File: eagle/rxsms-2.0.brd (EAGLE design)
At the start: 160 x 100 mm, 13 parts, among them U1 MAX3232ESE, U2 XMEGA-A4UTQFP, X1 PN61729-S

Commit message: continued schematics
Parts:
- added C10, C11: opt, rcl:C0805K
- added C12, C13: 4u7/50V, rcl:C0805K
- added C14, C15: 22u/16V, rcl:C0805K
- added C16, C21, C22, C23, C24, C25, C26, C27, C28, C29, C6, C7, C8, C9: 100n, rcl:C0805K
- added C17, C18, C19, C20: >100n/low ESR, rcl:C0805K
- added Q1: opt, crystal:HC49/S
- added Q2, Q3, Q4: BSS123, transistor-small-signal:SOT23
- added R1, R10, R11, R2, R3, R4, R5, R6, R8, R9: 10k, rcl:R0805
- added R12, R13, R14, R15: 24/1%, rcl:R0805
- added R16, R17, R18, R19, R20: 1k, rcl:R0805
- added R7: 100k, rcl:R0805
- added T1, T2, T3, T4, T5: SMS_IP67, SMSIp67:IP67
- added U$3: AVR-PDIVERT, avr-7:AVR-ISP-6
- added U$4: UDN2596, UDN2596:DIL20
- added U$5: SP490, SP491:SO08
- added U$6: BTS6143, BTS6134:TO-252-5-1
- added U$7, U$8, U$9: (no value), poti:VERT_POTI
- added U3: TSR_1-2450, _traco_tsr-1:TSR-1
- added U4: LM1117, LM1117:TO252
- added U5: TMV_0505EN, _traco_tmv-1:TMV-EN
- added U6: ADUM3160, adum3160:SO-16W
- added U7: TPS73125, TPS731xx:SOT25
- moved X1 394.7 mm to (-191.8, -289.6), turned to 0 degrees
- moved X4 288.8 mm to (-80.0, -123.2)
- moved U2 44.4 mm to (-87.6, 22.9), turned to 180 degrees
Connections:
- removed net AVCC: U2.39
- removed net VCC: U2.19, U2.31, U2.9
- new net !EXP_LO: U$4.16, X4.5
- new net !EXP_SODS: U$4.15, X4.3
- new net !EXP_SOE: U$4.17, X4.4
- new net !SIM_LO: R4.1, U$4.19
- new net !SIM_SODS: R2.1, U$4.13
- new net !SIM_SOE: R3.1, U$4.18
- new net +28V_EXP: U$4.10, U$6.PIN1, U$6.PIN5, X4.1, X4.9
- new net +28V_SUPPLY: C12.1, U$6.TAB
- new net +3V3: C15.1, C19.1, C20.1, C6.1, C7.1, C8.1, C9.1, Q3.1, Q4.1, R1.1, R10.2, R2.2, R3.2, R4.2, R8.2, U$3.2, U$4.20, U2.19, U2.31, U2.39, U2.9, U4.3, U6.12, U6.13, U6.14, U6.16
- new net +5V: C13.1, C14.1, C16.1, R11.2, R9.2, U$5.1, U3.3, U4.2, U5.1, U7.1, U7.3
- new net ADC_POTI_BIT_ERROR_RATE: C22.1, U$7.P2
- new net ADC_POTI_DROP_DURATION: C24.1, U$9.P2
- new net ADC_POTI_DROP_RATE: C23.1, U$8.P2
- new net EXPPWR_EN: Q2.1, R5.2
- new net EXP_CHG_IN: X4.2
- new net EXP_CHG_RET: X4.12
- new net EXP_SERIAL_FROM_EXP+: R6.2, U$5.8, X4.13
- new net EXP_SERIAL_FROM_EXP-: R6.1, U$5.7, X4.14
- new net EXP_SERIAL_TO_EXP+: R7.1, U$5.5, X4.6
- new net EXP_SERIAL_TO_EXP-: R7.2, U$5.6, X4.7
- new net N$11: C10.1, Q1.1, U2.37
- new net N$12: C11.1, Q1.2, U2.36
- new net N$13: U$3.1, U2.34
- new net N$14: R1.2, U$3.5, U2.35
- new net N$15: C17.2, C18.2, U6.2, U6.8, X1.4, X1.S1, X1.S2
- new net N$16: Q2.3, U$6.PIN2
- new net N$17: C18.1, U6.1, X1.1
- new net N$18: C17.1, U6.3, U6.4, U6.5
- new net N$19: R12.1, U6.6
- new net N$20: Q3.3, R9.1, U$5.2
- new net N$21: Q4.3, R11.1, U$5.3
- new net N$22: R13.1, U6.7
- new net N$23: R13.2, X1.3
- new net N$24: R12.2, X1.2
- new net N$25: C21.1, U7.4
- new net N$26: C25.2, T1.1, T1.2
- new net N$27: C26.2, T2.1, T2.2
- new net N$28: R17.1, T2.3, T2.4
- new net N$29: R14.2, U6.9
- new net N$30: R15.2, U6.10
- new net N$31: R16.1, T1.3, T1.4
- new net N$32: C27.2, T3.1, T3.2
- new net N$33: R18.1, T3.3, T3.4
- new net N$34: C28.2, T4.1, T4.2
- new net N$35: R19.1, T4.3, T4.4
- new net N$36: C29.2, T5.1, T5.2
- new net N$37: R20.1, T5.3, T5.4
- new net N$38: U$7.P3, U$8.P3, U$9.P3, U7.5
- new net SW_ERRINH: C29.1, R20.2
- new net SW_LO: C25.1, R16.2
- new net SW_PWR: C28.1, R19.2
- new net SW_SODS: C27.1, R18.2
- new net SW_SOE: C26.1, R17.2
- new net UART_EXP_RX: Q3.2, R8.1
- new net UART_EXP_TX: Q4.2, R10.1
- new net USB-D+: R15.1
- new net USB_D-: R14.1
- net GND: now also C10.2, C11.2, C12.2, C13.2, C14.2, C15.2, C16.2, C19.2, C20.2, C21.2, C22.2, C23.2, C24.2, C6.2, C7.2, C8.2, C9.2, Q2.2, R5.1, U$3.6, U$4.12, U$4.2, U$5.4, U$7.P1, U$8.P1, U$9.P1, U3.2, U4.1, U5.2, U6.11, U6.15, U7.2, X4.15, X4.8, X4.G1, X4.G2
- net VDD: now also U5.5
- net VSS: now also U5.7

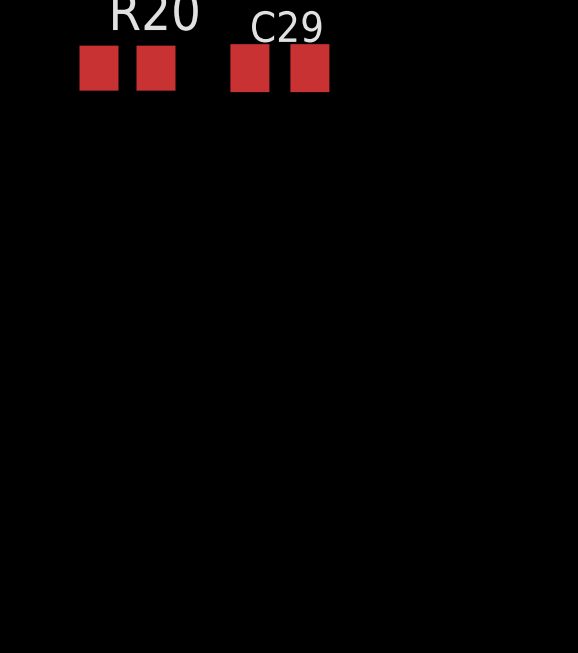
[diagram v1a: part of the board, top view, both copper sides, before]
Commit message: capacitors for isolating DCDC converter added
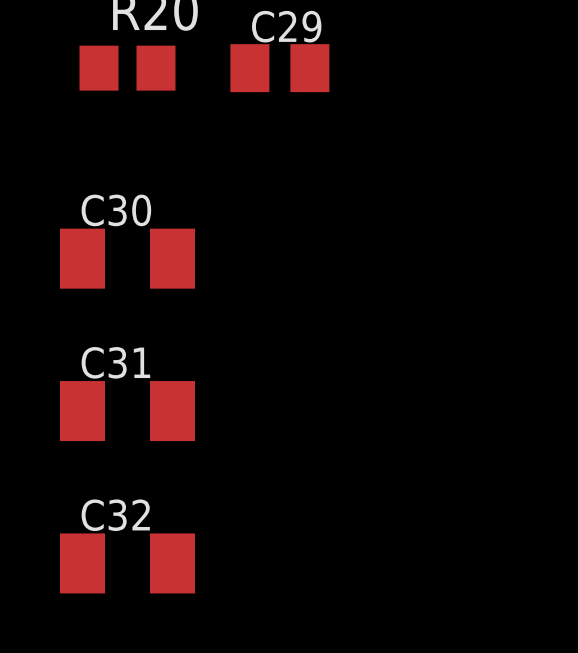
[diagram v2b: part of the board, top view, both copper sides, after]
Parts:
- added C30, C31, C32: 10u/16V, rcl:C1206K
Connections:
- new net +VIN: C31.1, U5.1
- net +5V: now also C30.1; no longer U5.1
- net GND: now also C30.2, C31.2
- net VDD: now also C32.1
- net VSS: now also C32.2
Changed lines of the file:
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@@
 <element name="R20" library="rcl" package="R0805" value="1k" x="-224.79" y="-469.9"/>
 <element name="C29" library="rcl" package="C0805K" value="100n" x="-219.71" y="-469.9"/>
+<element name="C30" library="rcl" package="C1206K" value="10u/16V" x="-224.79" y="-476.25"/>
+<element name="C31" library="rcl" package="C1206K" value="10u/16V" x="-224.79" y="-481.33"/>
+<element name="C32" library="rcl" package="C1206K" value="10u/16V" x="-224.79" y="-486.41"/>
 </elements>
 <signals>
@@
 <contactref element="C23" pad="2"/>
 <contactref element="C24" pad="2"/>
+<contactref element="C30" pad="2"/>
+<contactref element="C31" pad="2"/>
 <wire x1="-210.76" y1="-306.91" x2="-196.85" y2="-306.1" width="0" layer="19" extent="1-1"/>
 <wire x1="-211.09" y1="-311.15" x2="-210.76" y2="-306.91" width="0" layer="19" extent="1-1"/>
@@
 <wire x1="-81.83" y1="24.46" x2="-88.43" y2="28.66" width="0" layer="19" extent="1-1"/>
 <wire x1="-154.305" y1="-146.5834" x2="-131.76" y2="-175.26" width="0" layer="19" extent="1-1"/>
+<wire x1="-223.29" y1="-476.25" x2="-211.09" y2="-365.76" width="0" layer="19" extent="1-1"/>
+<wire x1="-223.29" y1="-481.33" x2="-223.29" y2="-476.25" width="0" layer="19" extent="1-1"/>
 </signal>
 <signal name="VSS">
@@
 <contactref element="X2" pad="G2"/>
 <contactref element="U5" pad="7"/>
+<contactref element="C32" pad="2"/>
+<wire x1="-83.82" y1="-78.74" x2="-223.29" y2="-486.41" width="0" layer="19" extent="1-1"/>
 <wire x1="11.43" y1="12.8778" x2="-83.82" y2="-78.74" width="0" layer="19" extent="1-1"/>
 <wire x1="12.7" y1="30.8864" x2="11.43" y2="12.8778" width="0" layer="19" extent="1-1"/>
@@
 <contactref element="C1" pad="1"/>
 <contactref element="U5" pad="5"/>
+<contactref element="C32" pad="1"/>
+<wire x1="-88.9" y1="-78.74" x2="-226.29" y2="-486.41" width="0" layer="19" extent="1-1"/>
 <wire x1="-49.26" y1="80.01" x2="-88.9" y2="-78.74" width="0" layer="19" extent="1-1"/>
 <wire x1="-42.545" y1="84.3534" x2="-49.26" y2="80.01" width="0" layer="19" extent="1-1"/>
@@
 <contactref element="C13" pad="1"/>
 <contactref element="C14" pad="1"/>
-<contactref element="U5" pad="1"/>
 <contactref element="U$5" pad="1"/>
 <contactref element="C16" pad="1"/>
@@
 <contactref element="U7" pad="1"/>
 <contactref element="U7" pad="3"/>
+<contactref element="C30" pad="1"/>
 <wire x1="-195.9" y1="-306.1" x2="-197.8" y2="-306.1" width="0" layer="19" extent="1-1"/>
 <wire x1="-175.52" y1="-298.17" x2="-195.9" y2="-306.1" width="0" layer="19" extent="1-1"/>
@@
 <wire x1="-131.81" y1="-194.31" x2="-129.86" y2="-214.63" width="0" layer="19" extent="1-1"/>
 <wire x1="-158.115" y1="-146.5834" x2="-131.81" y2="-194.31" width="0" layer="19" extent="1-1"/>
-<wire x1="-99.06" y1="-78.74" x2="-158.115" y2="-146.5834" width="0" layer="19" extent="1-1"/>
-<wire x1="-101.33" y1="-66.04" x2="-99.06" y2="-78.74" width="0" layer="19" extent="1-1"/>
+<wire x1="-101.33" y1="-66.04" x2="-158.115" y2="-146.5834" width="0" layer="19" extent="1-1"/>
 <wire x1="-101.33" y1="-60.96" x2="-101.33" y2="-66.04" width="0" layer="19" extent="1-1"/>
 <wire x1="-82.55" y1="-48.26" x2="-101.33" y2="-60.96" width="0" layer="19" extent="1-1"/>
+<wire x1="-226.29" y1="-476.25" x2="-197.8" y2="-306.1" width="0" layer="19" extent="1-1"/>
 </signal>
 <signal name="!SIM_LO">
@@
 <wire x1="-205.76" y1="-351.36" x2="-205.76" y2="-332.31" width="0" layer="19" extent="1-1"/>
 </signal>
+<signal name="+VIN">
+<contactref element="U5" pad="1"/>
+<contactref element="C31" pad="1"/>
+<wire x1="-99.06" y1="-78.74" x2="-226.29" y2="-481.33" width="0" layer="19" extent="1-1"/>
+</signal>
 </signals>

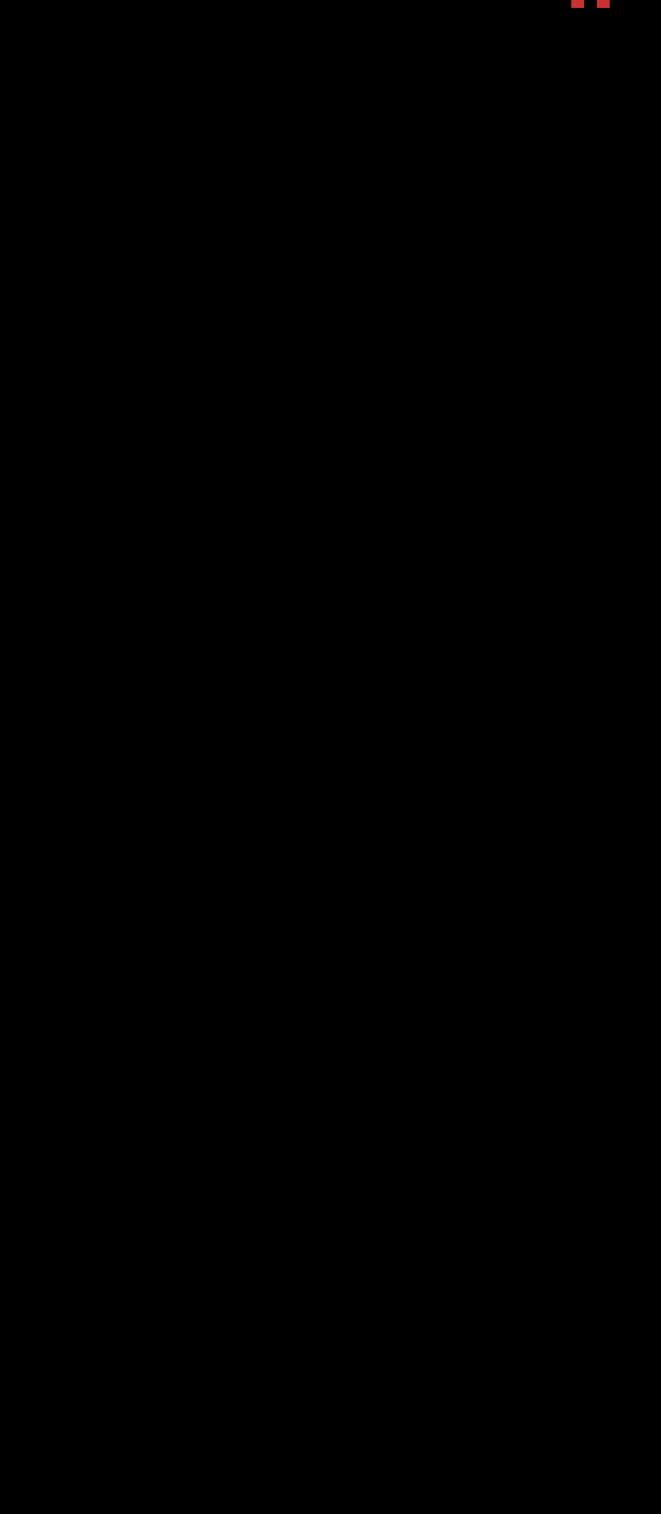
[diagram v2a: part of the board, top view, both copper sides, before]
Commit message: added optocouplers for MAX3232
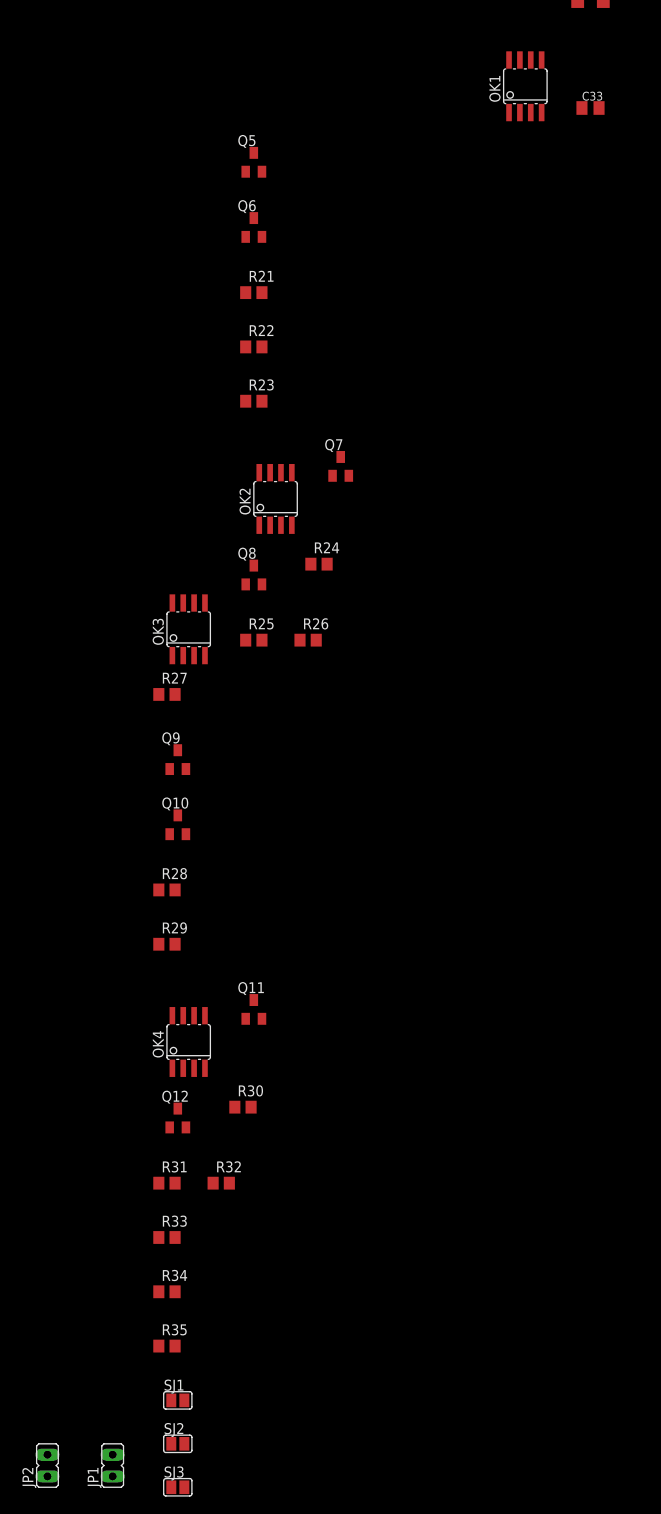
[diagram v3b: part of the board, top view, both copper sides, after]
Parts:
- added C33: 100n, rcl:C0805K
- added JP1, JP2: (no value), jumper:JP1
- added OK1, OK2, OK3, OK4: HCPL0600, optocoupler:SOIC08
- added Q10, Q11, Q12, Q5, Q6, Q7, Q8, Q9: BSS123, transistor-small-signal:SOT23
- added R21, R23, R24, R26, R27, R28, R30, R31: 10k, rcl:R0805
- added R22, R25: 127, rcl:R0805
- added R29, R32: 267, rcl:R0805
- added R33, R34, R35: opt, rcl:R0805
- added SJ1, SJ2, SJ3: (no value), jumper:SJ
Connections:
- new net ADC_REF: C33.1, U$7.P3, U$8.P3, U$9.P3, U7.5
- new net DEBUG_RX_D-: R33.1
- new net DEBUG_TX_D+: R35.1
- new net N$39: OK1.6, R23.1, U1.11
- new net N$40: Q5.1, Q6.3, R21.1
- new net N$41: Q11.1, Q12.3, R31.1
- new net N$42: OK1.2, R22.1
- new net N$43: OK2.3, Q7.3
- new net N$44: OK2.2, R25.1
- new net N$45: OK2.6, R26.1, U1.10
- new net N$46: Q7.1, Q8.3, R24.1
- new net N$47: Q10.3, Q9.1, R28.1
- new net N$48: OK3.3, Q9.3
- new net N$49: OK4.3, Q11.3
- new net N$50: OK3.2, R29.1
- new net N$51: OK4.2, R32.1
- new net N$52: Q10.1, U1.12
- new net N$53: Q12.1, U1.9
- new net N$54: OK4.6, R30.1, R33.2
- new net N$55: Q8.1, R34.2, R35.2
- new net N$56: SJ1.2, X2.G2
- new net N$57: SJ2.2, X3.G2
- new net N$58: SJ3.2, X4.G2
- new net N$59: JP1.2, JP2.1, R34.1
- new net UART_GND_RX: OK3.6, R27.1
- new net UART_GND_TX: Q6.1
- net +3V3: now also OK3.7, OK3.8, OK4.7, OK4.8, R21.2, R22.2, R24.2, R25.2, R27.2, R30.2
- net GND: now also C33.2, OK3.5, OK4.5, Q5.2, Q6.2, Q7.2, Q8.2, SJ3.1; no longer X4.G1, X4.G2
- net N$38: now also OK1.3, Q5.3; no longer U$7.P3, U$8.P3, U$9.P3, U7.5
- net UART_EXP_RX: now also JP1.1
- net UART_EXP_TX: now also JP2.2
- net VDD: now also OK1.7, OK1.8, OK2.7, OK2.8, R23.2, R26.2, R28.2, R29.2, R31.2, R32.2
- net VSS: now also OK1.5, OK2.5, Q10.2, Q11.2, Q12.2, Q9.2, SJ1.1, SJ2.1; no longer X2.G1, X2.G2, X3.G1, X3.G2

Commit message: added RX EXP charging line to debug serial DSUB
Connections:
- net EXP_CHG_IN: now also X3.1, X3.6, X3.7
- net EXP_CHG_RET: now also X3.4, X3.8, X3.9
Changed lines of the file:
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@@
 <signal name="EXP_CHG_IN">
 <contactref element="X4" pad="2"/>
+<contactref element="X3" pad="1"/>
+<contactref element="X3" pad="6"/>
+<contactref element="X3" pad="7"/>
+<wire x1="12.7" y1="68.1736" x2="-81.28" y2="-116.332" width="0" layer="19" extent="1-1"/>
+<wire x1="10.16" y1="69.5452" x2="12.7" y2="68.1736" width="0" layer="19" extent="1-1"/>
+<wire x1="10.16" y1="72.2884" x2="10.16" y2="69.5452" width="0" layer="19" extent="1-1"/>
 </signal>
 <signal name="EXP_CHG_RET">
 <contactref element="X4" pad="12"/>
+<contactref element="X3" pad="4"/>
+<contactref element="X3" pad="8"/>
+<contactref element="X3" pad="9"/>
+<wire x1="10.16" y1="75.0316" x2="-78.74" y2="-123.19" width="0" layer="19" extent="1-1"/>
+<wire x1="10.16" y1="77.7748" x2="10.16" y2="75.0316" width="0" layer="19" extent="1-1"/>
+<wire x1="12.7" y1="76.4032" x2="10.16" y2="75.0316" width="0" layer="19" extent="1-1"/>
 </signal>
 <signal name="N$17">

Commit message: second set of buttons and LEDs added
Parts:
- added LED1, LED2, LED3, LED4, LED5, LED6, LED7, LED8: (no value), led:CHIPLED_1206
- added R36, R37, R38, R39, R40, R41, R42, R43, R44, R45, R46, R47: 220, rcl:R0805
- added T10, T6, T7, T8: SWITCH_LED, mentor-switch:SWITCH_LED
- added T9: SMS_IP67, SMSIp67:IP67
- T3: value SMS_IP67 -> SWITCH_LED; device SMSIp67:IP67 -> mentor-switch:SWITCH_LED
- moved T1 495.7 mm to (-349.2, -838.2)
- moved T4 418.8 mm to (-336.6, -838.2)
- moved T5 393.4 mm to (-323.9, -838.2)
- moved R16 371.5 mm to (-289.6, -737.9)
- moved C25 362.1 mm to (-278.1, -736.6)
- moved R18 354.0 mm to (-289.6, -772.2)
- moved C27 352.7 mm to (-284.5, -770.9)
- moved R17 341.6 mm to (-283.2, -737.9)
- moved C26 339.5 mm to (-273.1, -736.6)
- moved T2 318.0 mm to (-273.1, -703.6)
- moved T3 308.2 mm to (-266.7, -717.5)
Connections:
- new net LED_ERRINH: R42.1, R43.1
- new net LED_LO: R36.1, R37.1
- new net LED_TO_EXP_ACTIVE: R46.2
- new net LED_TO_GND_ACTIVE: R47.2
- new net N$60: R41.1
- new net N$61: LED4.A, R43.2
- new net N$62: R42.2, T7.A
- new net N$63: LED5.A, R44.2
- new net N$64: R45.2, T6.A
- new net N$65: LED6.A, R46.1
- new net N$66: LED7.A, R47.1
- net !SIM_SODS: now also LED3.C, T10.K
- net !SIM_SOE: now also LED2.C, T3.K
- net +3V3: now also LED8.A, R38.2, R39.1, R40.1, R41.2
- net EXPPWR_EN: now also R44.1, R45.1
- net GND: now also C25.2, C26.2, C27.2, C28.2, C29.2, LED1.C, LED4.C, LED5.C, LED6.C, LED7.C, LED8.C, T1.1, T1.2, T10.3A, T2.1, T2.2, T3.3A, T4.1, T4.2, T5.1, T5.2, T6.3A, T6.K, T7.3A, T7.K, T8.3A, T8.K, T9.1, T9.2
- net N$26: now also R16.1, T1.3, T1.4, T8.A1; no longer C25.2, T1.1, T1.2
- net N$27: now also R17.1, T2.3, T2.4, T3.A1; no longer C26.2, T2.1, T2.2
- net N$28: now also R18.1, T10.A1, T9.3, T9.4; no longer R17.1, T2.3, T2.4
- net N$31: now also LED1.A, R37.2; no longer R16.1, T1.3, T1.4
- net N$32: now also R36.2, T8.A; no longer C27.2, T3.1, T3.2
- net N$33: now also LED2.A, R39.2; no longer R18.1, T3.3, T3.4
- net N$34: now also R38.1; no longer C28.2, T4.1, T4.2
- net N$35: now also T6.A1
- net N$36: now also LED3.A, R40.2; no longer C29.2, T5.1, T5.2
- net N$37: now also T7.A1
